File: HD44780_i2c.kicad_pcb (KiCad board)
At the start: 2 copper layers, 23 x 48 mm, 13 parts, among them IC1 PI4IOE5V6416LEX, J1 Conn_01x05_Male, J2 Conn_01x02_Male, J4 Conn_01x18_Male, Q1 Q_NPN_BCE

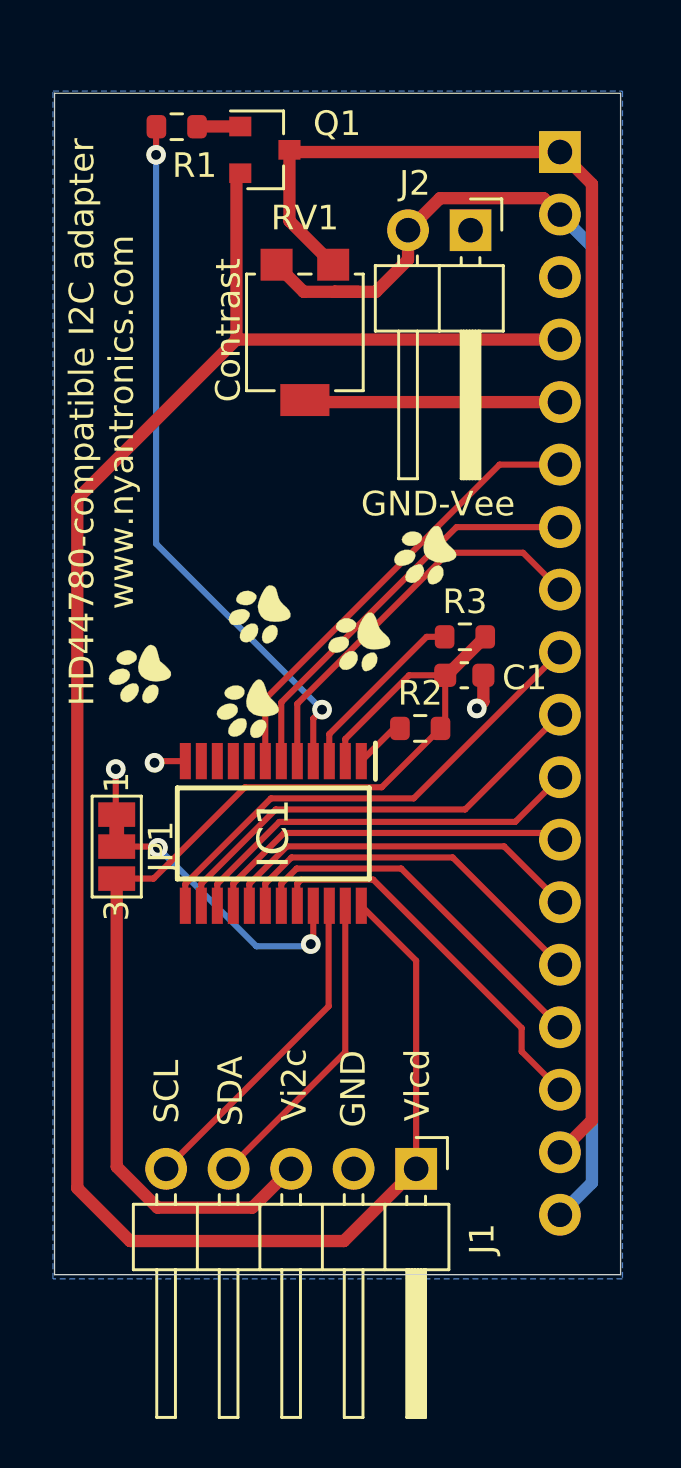
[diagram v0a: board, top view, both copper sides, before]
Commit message: Replace main IC with Ti version. Reroute PCB. Update silkscreen.
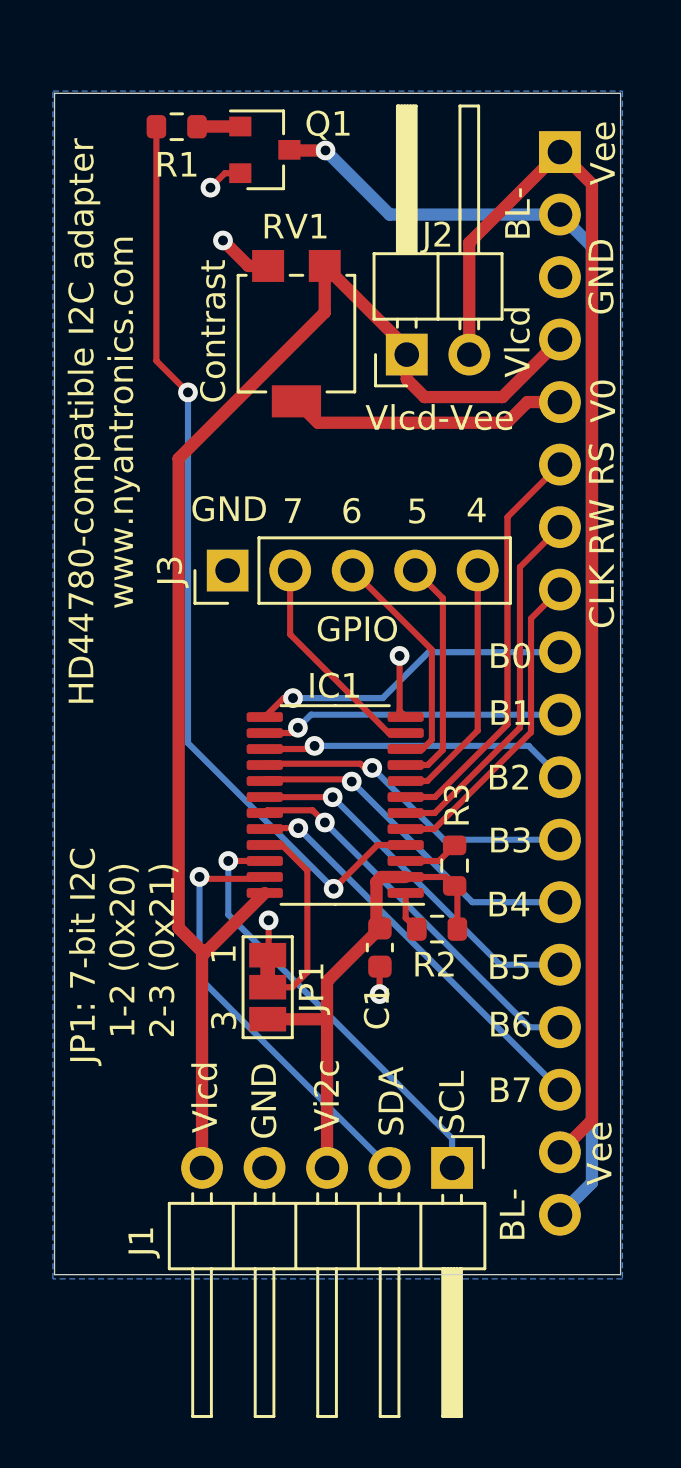
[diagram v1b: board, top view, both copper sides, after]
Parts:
- removed the G*** at (159.2, 98.2)
- added J3: Conn_01x05, Connector_PinHeader_2.54mm:PinHeader_1x05_P2.54mm_Vertical, F.Cu at (157.0, 96.4)
- IC1: value PI4IOE5V6416LEX -> TCA6416APWR; footprint PI4IOE5V6416LEX:SOP65P640X120-24N -> Package_SO:TSSOP-24_4.4x7.8mm_P0.65mm
- moved C1 11.6 mm to (163.2, 111.7), turned to 270 degrees
- moved G*** 9.91 mm to (164.3, 109.0)
- moved R3 9.31 mm to (166.3, 108.4), turned to 270 degrees
- moved JP1 8.38 mm to (158.7, 113.3)
- moved R2 8.18 mm to (165.5, 111.0)
- moved J2 5.68 mm to (164.3, 87.6), turned to 90 degrees
- moved IC1 2.77 mm to (161.4, 105.9), turned to 180 degrees
- moved J1 1.46 mm to (166.2, 120.7)
- moved RV1 0.35 mm to (159.8, 86.8)
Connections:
- J1 pad 1: Vlcd -> SCL
- J1 pad 2: GND -> SDA
- J1 pad 4: SDA -> GND
- J1 pad 5: SCL -> Vlcd
- J2 pad 1: GND -> Vlcd
- J2 pad 2: BL_Vee -> Vee
- J4 pad 1: Vlcd_bl -> Vee
- J4 pad 17: Vlcd_bl -> Vee
- J4 pad 18: BL_Vee -> GND_bl
- J4 pad 2: BL_Vee -> GND_bl
- Q1 pad 2: Vlcd -> GND
- Q1 pad 3: Vlcd_bl -> GND_bl
- RV1 pad 1: Vlcd_bl -> Vlcd
- RV1 pad 3: BL_Vee -> GND
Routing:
- net Vlcd_bl: track 58.2 -> 0.00 mm
- net BL_Vee: track 57.2 -> 0.00 mm
- net GND_bl: track 0.00 -> 53.8 mm, vias 0 -> 1
- net Vee: track 0.00 -> 51.5 mm
- net Vi2c: track 46.4 -> 20.2 mm
- net Vlcd: track 84.6 -> 61.5 mm
- net Net-(IC1-Pad8): track 0.00 -> 10.3 mm
- net Net-(IC1-Pad9): track 0.00 -> 9.52 mm
- net Net-(IC1-Pad10): track 0.00 -> 9.42 mm
- net Net-(IC1-Pad11): track 0.00 -> 8.95 mm
- net BL_TGL: track 28.7 -> 37.6 mm
- net B0: track 20.0 -> 13.1 mm, vias 0 -> 1
- net B1: track 18.3 -> 12.3 mm, vias 0 -> 1
- net Net-(IC1-Pad3): track 7.42 -> 2.25 mm
- net SDA: track 12.7 -> 17.7 mm, vias 0 -> 1
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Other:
- board text added: "4"
- board text added: "5"
- board text added: "6"
- board text added: "7"
- board text added: "B0"
- board text added: "B1"
- board text added: "B2"
- board text added: "B3"
- board text added: "B4"
- board text added: "B5"
- board text added: "B6"
- board text added: "B7"
- board text added: "BL-"
- board text added: "CLK"
- board text added: "GPIO"
- board text added: "JP1: 7-bit I2C 1-2 (0x20) 2-3 (0x21)"
- board text added: "RS"
- board text added: "RW"
- board text added: "V0"
- board text added: "Vee"
- board text added: "Vlcd-Vee"
- board text removed: "GND-Vee"

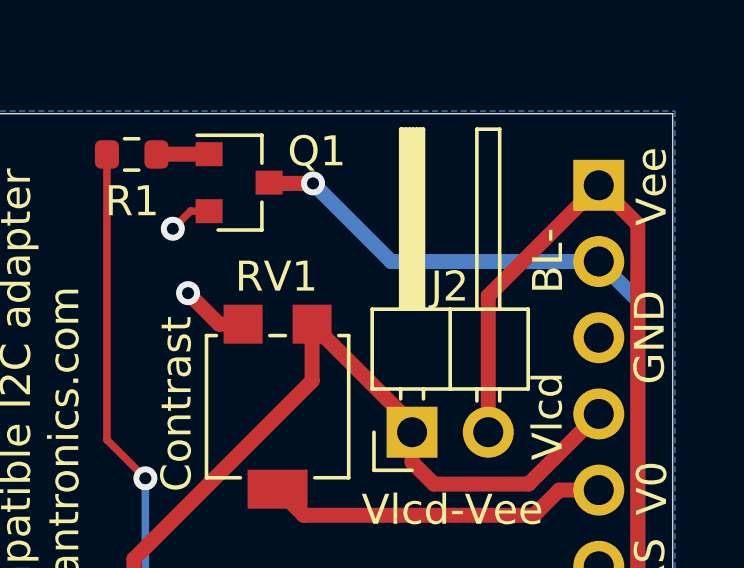
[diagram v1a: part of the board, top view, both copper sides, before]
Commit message: Add silkscreen docu.
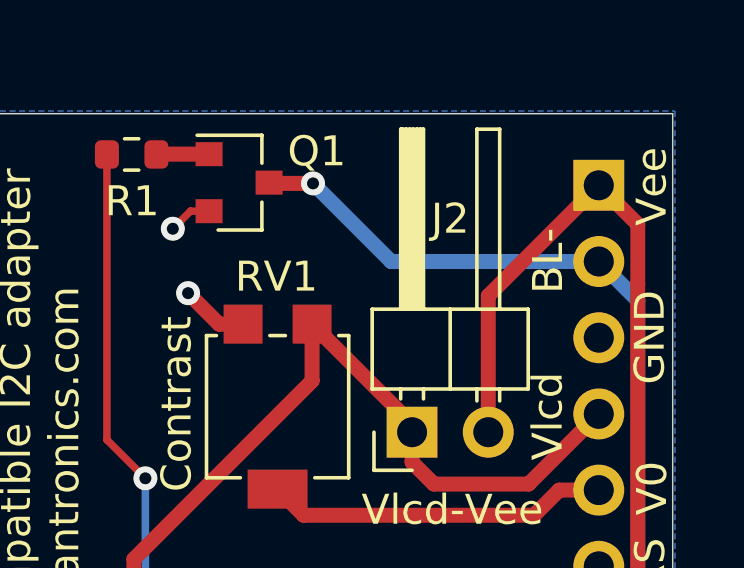
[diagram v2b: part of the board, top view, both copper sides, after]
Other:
- board text added: "Connect Vlcd-Vee (J2) if Vee is backlight +"
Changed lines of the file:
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@@
   (general
     (thickness 1.6)
-    (drawings 38)
+    (drawings 39)
     (tracks 167)
     (zones 0)
@@
     (descr "Through hole angled pin header, 1x02, 2.54mm pitch, 6mm pin length, single row")
     (tags "Through hole angled pin header THT 1x02 2.54mm single row")
-    (fp_text reference J2 (at 4.8514 1.2573 180) (layer F.SilkS)
+    (fp_text reference J2 (at 7.112 1.27 180) (layer F.SilkS)
       (effects (font (size 1 1) (thickness 0.15)))
     )
@@
     )
   )
+  (gr_text "Connect Vlcd-Vee (J2) \nif Vee is backlight +" (at 152.7556 87.1982 90) (layer B.SilkS)
+    (effects (font (size 1 1) (thickness 0.15)) (justify mirror))
+  )
   (gr_text "JP1: 7-bit I2C\n 1-2 (0x20)\n 2-3 (0x21)" (at 152.781 112.0394 90) (layer F.SilkS)

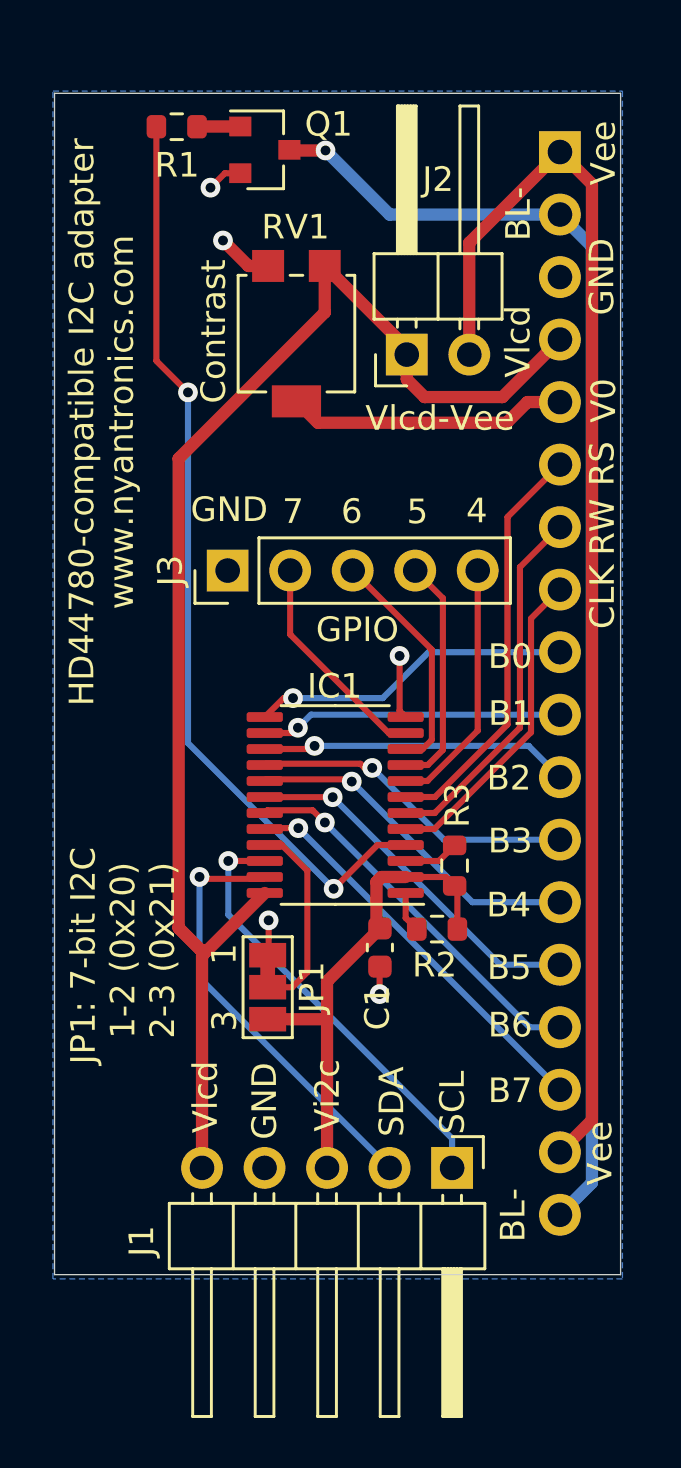
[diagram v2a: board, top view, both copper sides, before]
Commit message: Correctly orient main header. Update layout & routing.
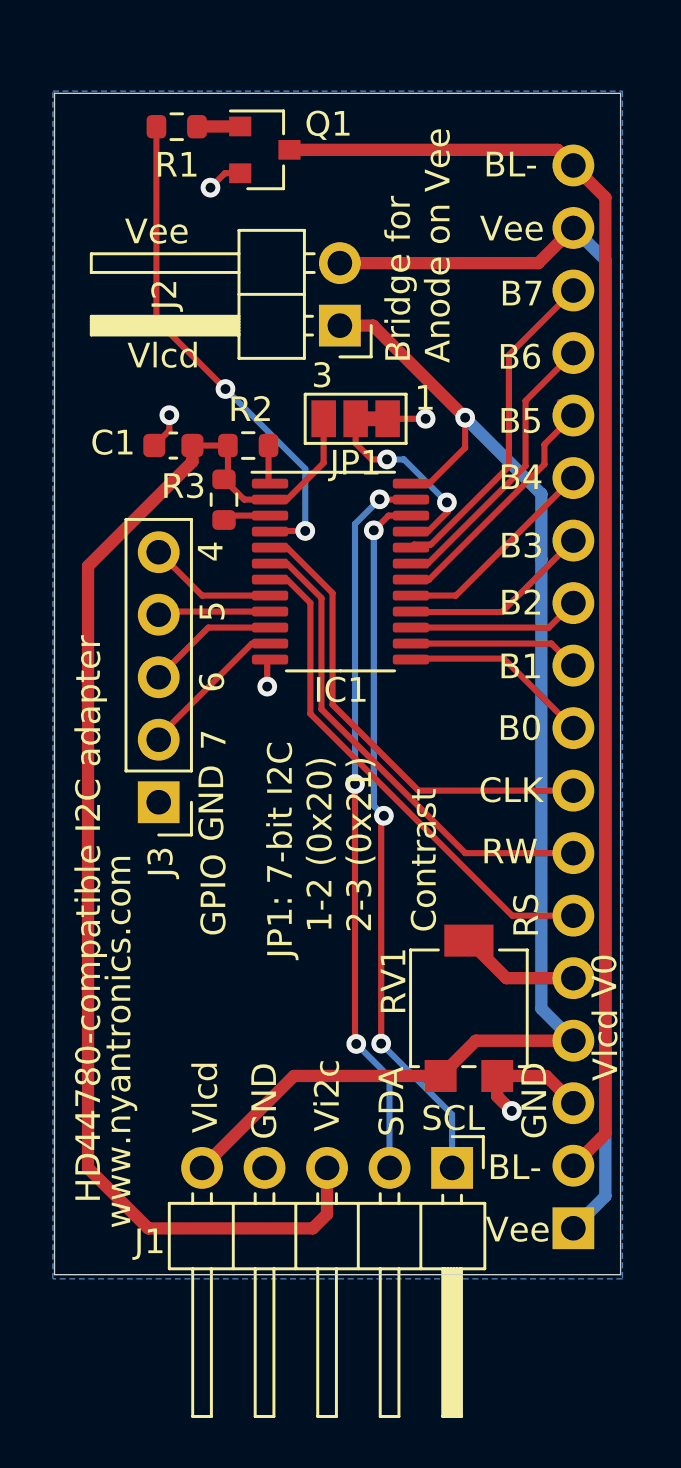
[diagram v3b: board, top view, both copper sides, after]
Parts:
- moved J4 43.7 mm to (171.1, 123.1), turned to 0 degrees
- moved RV1 28.3 mm to (166.8, 114.2), turned to 180 degrees
- moved JP1 23.4 mm to (162.2, 90.2), turned to 180 degrees
- moved C1 22.1 mm to (154.8, 91.3), turned to 180 degrees
- moved R2 21.1 mm to (157.9, 91.3), turned to 180 degrees
- moved R3 17.6 mm to (156.9, 93.5), turned to 90 degrees
- moved J3 9.82 mm to (154.2, 105.8), turned to 180 degrees
- moved IC1 9.49 mm to (161.6, 96.4), turned to 0 degrees
- moved G*** 4.55 mm to (160.0, 107.5)
- moved J2 2.96 mm to (161.6, 86.4), turned to 180 degrees
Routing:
- net Vi2c: track 20.2 -> 53.6 mm
- net BL_TGL: track 37.6 -> 20.4 mm
- net SDA: track 17.7 -> 29.4 mm, vias 1 -> 3
- net SCL: track 17.7 -> 29.1 mm, vias 1 -> 3
- net VO: track 11.4 -> 4.88 mm
- net Vlcd: track 61.5 -> 55.0 mm, vias 0 -> 1
- net CLK: track 13.0 -> 19.1 mm
- net B2: track 12.6 -> 7.01 mm, vias 1 -> 0
- net B4: track 14.1 -> 8.58 mm, vias 1 -> 0
- net B3: track 13.3 -> 7.81 mm, vias 1 -> 0
- net B1: track 12.3 -> 6.97 mm, vias 1 -> 0
- net B0: track 13.1 -> 7.79 mm, vias 1 -> 0
- net Net-(IC1-Pad8): track 10.3 -> 5.25 mm
- net B5: track 14.8 -> 9.84 mm, vias 1 -> 0
- net RW: track 14.9 -> 19.8 mm
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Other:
- board text added: "Bridge for Anode on Vee"
- board text added: "HD44780-compatible I2C adapter"
- board text removed: "HD44780-compatible I2C adapter www.nyantronics.com"
- board text removed: "Vlcd-Vee"

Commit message: Change location of jumper pad. Change Vi2c to VDD.
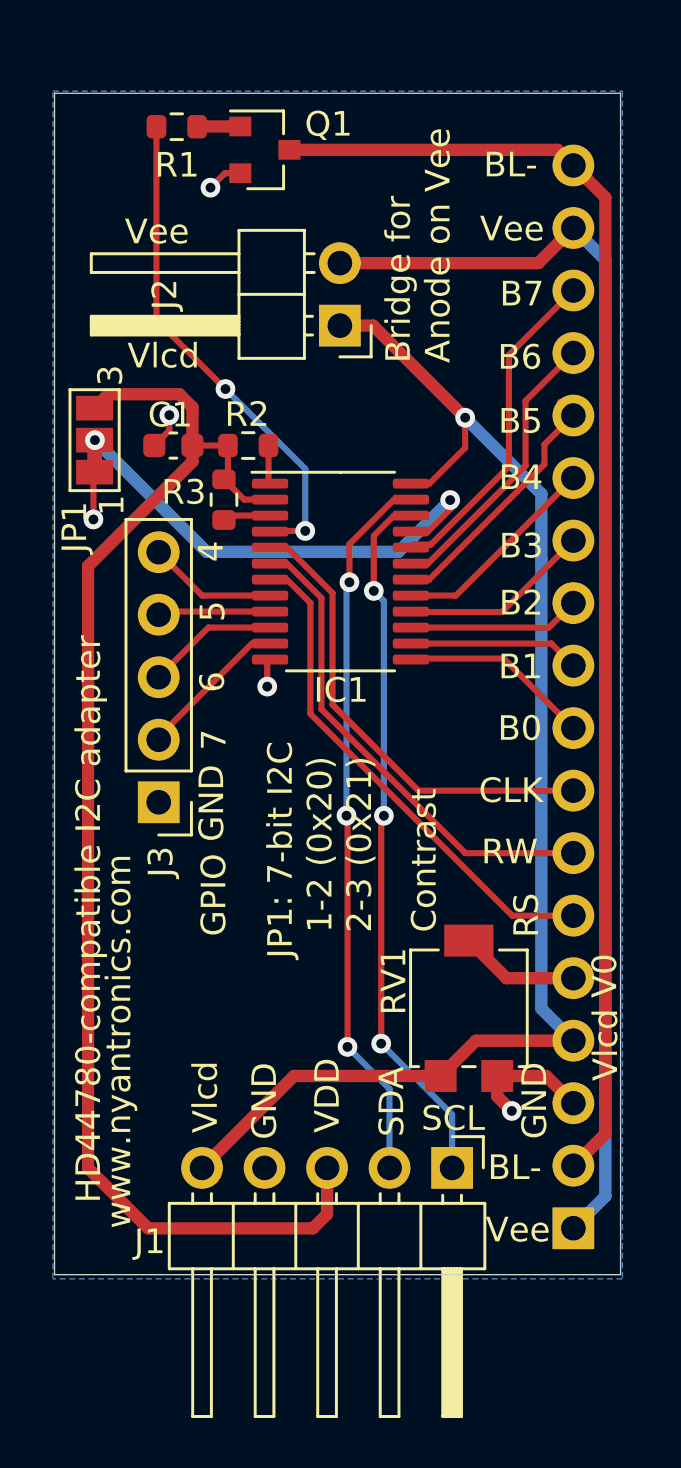
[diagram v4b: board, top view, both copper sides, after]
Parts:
- moved JP1 10.6 mm to (151.6, 91.1), turned to 90 degrees
- moved G*** 1.02 mm to (159.5, 108.4)
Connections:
- net Vi2c renamed VDD
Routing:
- net ADDR: track 7.93 -> 19.6 mm
- net VDD: track 53.6 -> 55.0 mm
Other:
- board text added: "VDD"
- board text removed: "Vi2c"
